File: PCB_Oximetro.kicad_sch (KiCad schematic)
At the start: 20 parts, among them J1 USB_A, J2 Conn_01x08, SW1 SW_Push, U1 LM1117MP-1.8, U2 MAX30102, U3 LM1117MP-3.3, U5 ESP32-DEVKIT-V1

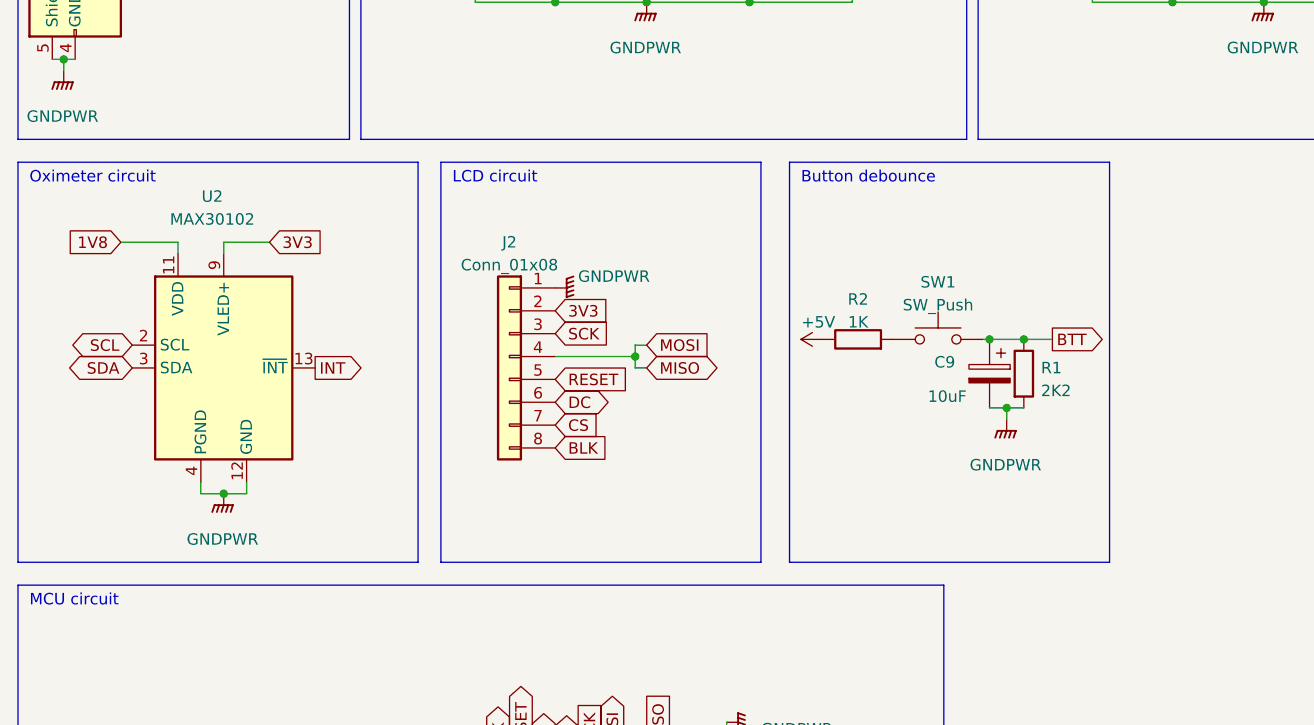
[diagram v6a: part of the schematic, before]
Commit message: I2C Adjust
Added I2C and INT pull up resistor
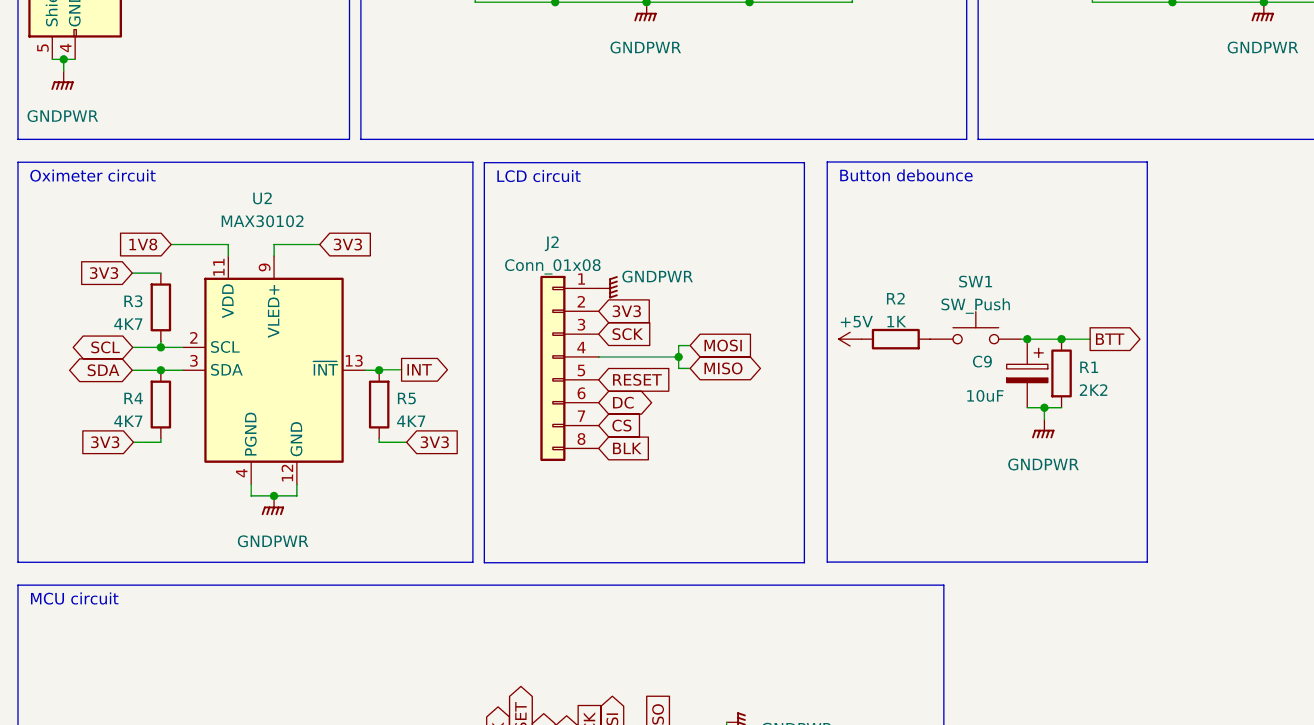
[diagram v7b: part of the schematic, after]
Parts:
- added R3, R4, R5: 4K7, Resistor_SMD:R_1206_3216Metric, symbol Device:R
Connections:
- net 3V3: now also R3.2, R4.1, R5.1
- net INT: now also R5.2
- net SCL: now also R3.1
- net SDA: now also R4.2
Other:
- moved on the sheet: C9, J2, R1, R2, SW1, U2

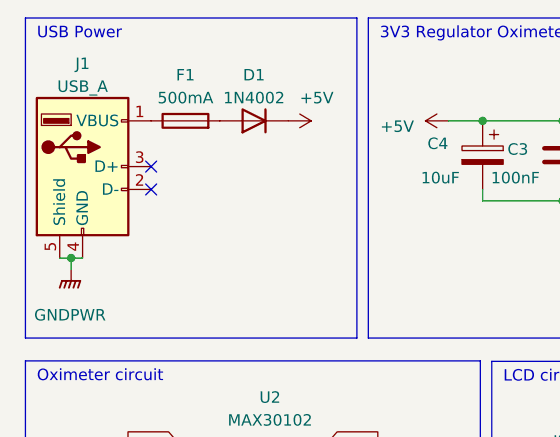
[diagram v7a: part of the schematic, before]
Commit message: USB change
Change USB for mini USB and removed fuse
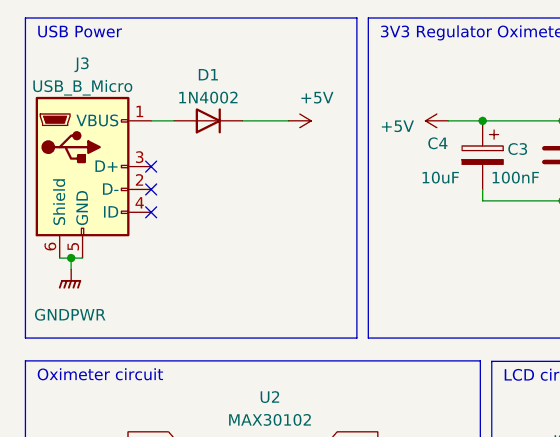
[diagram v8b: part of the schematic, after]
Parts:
- removed F1: 500mA, Fuse:Fuseholder_Cylinder-5x20mm_Stelvio-Kontek_PTF78_Horizontal_Open, symbol Device:Fuse
- removed J1: USB_A, Connector_USB:USB_A_Molex_67643_Horizontal, symbol Connector:USB_A
- added J3: USB_B_Micro, symbol Connector:USB_B_Micro
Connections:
- net GNDPWR: now also J3.5 (GND), J3.6 (Shield)
- net at D1.2 (A): now also J3.1 (VBUS)
- no-connect marks 18 -> 19
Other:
- moved on the sheet: D1
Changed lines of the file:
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@@
   (no_connect (at 67.31 121.92))
   (no_connect (at 52.07 152.4))
+  (no_connect (at 30.48 39.37))
   (no_connect (at 30.48 34.29))
   (no_connect (at 87.63 152.4))
@@
     (stroke (width 0) (type default))
   )
+  (wire (pts (xy 40.64 29.21) (xy 45.72 29.21))
+    (stroke (width 0) (type default))
+  )
   (wire (pts (xy 93.98 29.21) (xy 97.79 29.21))
     (stroke (width 0) (type default))
@@
   )
   (wire (pts (xy 42.418 92.964) (xy 44.958 92.964))
+    (stroke (width 0) (type default))
+  )
+  (wire (pts (xy 33.02 29.21) (xy 30.48 29.21))
     (stroke (width 0) (type default))
   )
@@
         (path "/885da8b5-ab69-4b52-8b49-00ecbcc643cb"
           (reference "R1") (unit 1)
+        )
+      )
+    )
+  )
+  (symbol (lib_id "Connector:USB_B_Micro") (at 22.86 34.29 0) (unit 1)
+    (in_bom yes) (on_board yes) (dnp no) (fields_autoplaced)
+    (property "Reference" "J3" (at 22.86 22.86 0)
+      (effects (font (size 1.27 1.27)))
+    )
+    (property "Value" "USB_B_Micro" (at 22.86 25.4 0)
+      (effects (font (size 1.27 1.27)))
+    )
+    (property "Footprint" "" (at 26.67 35.56 0)
+      (effects (font (size 1.27 1.27)) hide)
+    )
+    (property "Datasheet" "~" (at 26.67 35.56 0)
+      (effects (font (size 1.27 1.27)) hide)
+    )
+    (pin "1")
+    (pin "2")
+    (pin "3")
+    (pin "4")
+    (pin "5")
+    (pin "6")
+    (instances
+      (project "PCB_Oximetro"
+        (path "/885da8b5-ab69-4b52-8b49-00ecbcc643cb"
+          (reference "J3") (unit 1)
         )
       )
@@
     )
   )
-  (symbol (lib_id "Diode:1N4002") (at 41.91 29.21 180) (unit 1)
-    (in_bom yes) (on_board yes) (dnp no) (fields_autoplaced)
-    (property "Reference" "D1" (at 41.91 24.13 0)
-      (effects (font (size 1.27 1.27)))
-    )
-    (property "Value" "1N4002" (at 41.91 26.67 0)
-      (effects (font (size 1.27 1.27)))
-    )
-    (property "Footprint" "Diode_THT:D_DO-41_SOD81_P10.16mm_Horizontal" (at 41.91 24.765 0)
-      (effects (font (size 1.27 1.27)) hide)
-    )
-    (property "Datasheet" "http://www.vishay.com/docs/88503/1n4001.pdf" (at 41.91 29.21 0)
-      (effects (font (size 1.27 1.27)) hide)
-    )
-    (property "Sim.Device" "D" (at 41.91 29.21 0)
-      (effects (font (size 1.27 1.27)) hide)
-    )
-    (property "Sim.Pins" "1=K 2=A" (at 41.91 29.21 0)
+  (symbol (lib_id "Diode:1N4002") (at 36.83 29.21 180) (unit 1)
+    (in_bom yes) (on_board yes) (dnp no) (fields_autoplaced)
+    (property "Reference" "D1" (at 36.83 24.13 0)
+      (effects (font (size 1.27 1.27)))
+    )
+    (property "Value" "1N4002" (at 36.83 26.67 0)
+      (effects (font (size 1.27 1.27)))
+    )
+    (property "Footprint" "Diode_THT:D_DO-41_SOD81_P10.16mm_Horizontal" (at 36.83 24.765 0)
+      (effects (font (size 1.27 1.27)) hide)
+    )
+    (property "Datasheet" "http://www.vishay.com/docs/88503/1n4001.pdf" (at 36.83 29.21 0)
+      (effects (font (size 1.27 1.27)) hide)
+    )
+    (property "Sim.Device" "D" (at 36.83 29.21 0)
+      (effects (font (size 1.27 1.27)) hide)
+    )
+    (property "Sim.Pins" "1=K 2=A" (at 36.83 29.21 0)
       (effects (font (size 1.27 1.27)) hide)
     )
@@
         (path "/885da8b5-ab69-4b52-8b49-00ecbcc643cb"
           (reference "C8") (unit 1)
-        )
-      )
-    )
-  )
-  (symbol (lib_id "Connector:USB_A") (at 22.86 34.29 0) (unit 1)
-    (in_bom yes) (on_board yes) (dnp no) (fields_autoplaced)
-    (property "Reference" "J1" (at 22.86 22.86 0)
-      (effects (font (size 1.27 1.27)))
-    )
-    (property "Value" "USB_A" (at 22.86 25.4 0)
-      (effects (font (size 1.27 1.27)))
-    )
-    (property "Footprint" "Connector_USB:USB_A_Molex_67643_Horizontal" (at 26.67 35.56 0)
-      (effects (font (size 1.27 1.27)) hide)
-    )
-    (property "Datasheet" " ~" (at 26.67 35.56 0)
-      (effects (font (size 1.27 1.27)) hide)
-    )
-    (pin "1")
-    (pin "2")
-    (pin "3")
-    (pin "4")
-    (pin "5")
-    (instances
-      (project "PCB_Oximetro"
-        (path "/885da8b5-ab69-4b52-8b49-00ecbcc643cb"
-          (reference "J1") (unit 1)
         )
       )
@@
         )
       )
-    )
-  )
-  (symbol (lib_id "Device:Fuse") (at 34.29 29.21 90) (unit 1)
-    (in_bom yes) (on_board yes) (dnp no) (fields_autoplaced)
-    (property "Reference" "F1" (at 34.29 24.13 90)
-      (effects (font (size 1.27 1.27)))
-    )
-    (property "Value" "500mA" (at 34.29 26.67 90)
-      (effects (font (size 1.27 1.27)))
-    )
-    (property "Footprint" "Fuse:Fuseholder_Cylinder-5x20mm_Stelvio-Kontek_PTF78_Horizontal_Open" (at 34.29 30.988 90)
-      (effects (font (size 1.27 1.27)) hide)
-    )
-    (property "Datasheet" "~" (at 34.29 29.21 0)
-      (effects (font (size 1.27 1.27)) hide)
-    )
-    (pin "1")
-    (pin "2")
-    (instances
-      (project "PCB_Oximetro"
-        (path "/885da8b5-ab69-4b52-8b49-00ecbcc643cb"
-          (reference "F1") (unit 1)
-        )
-      )
